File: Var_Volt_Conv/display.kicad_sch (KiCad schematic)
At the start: 9 parts

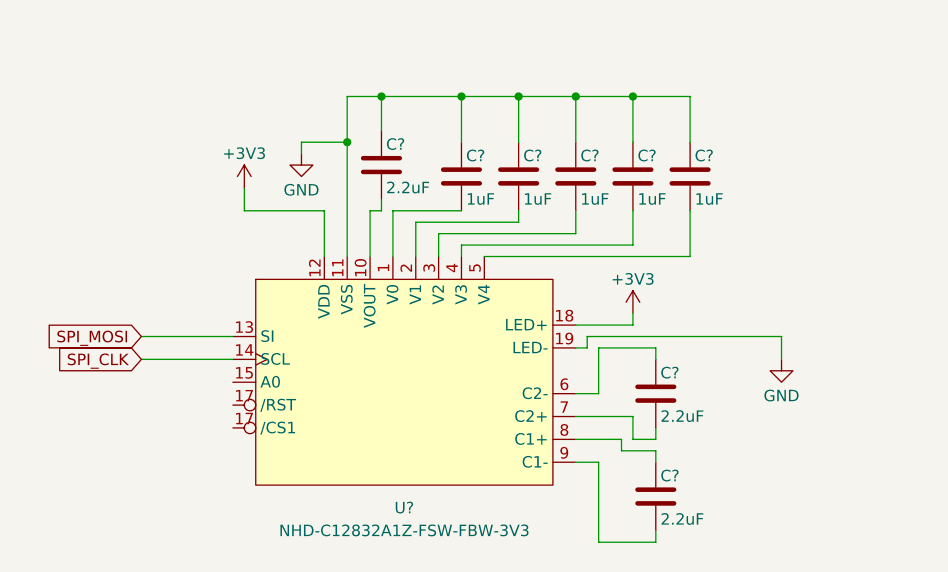
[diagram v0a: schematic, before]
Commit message: Tidied up microcontoller schematic
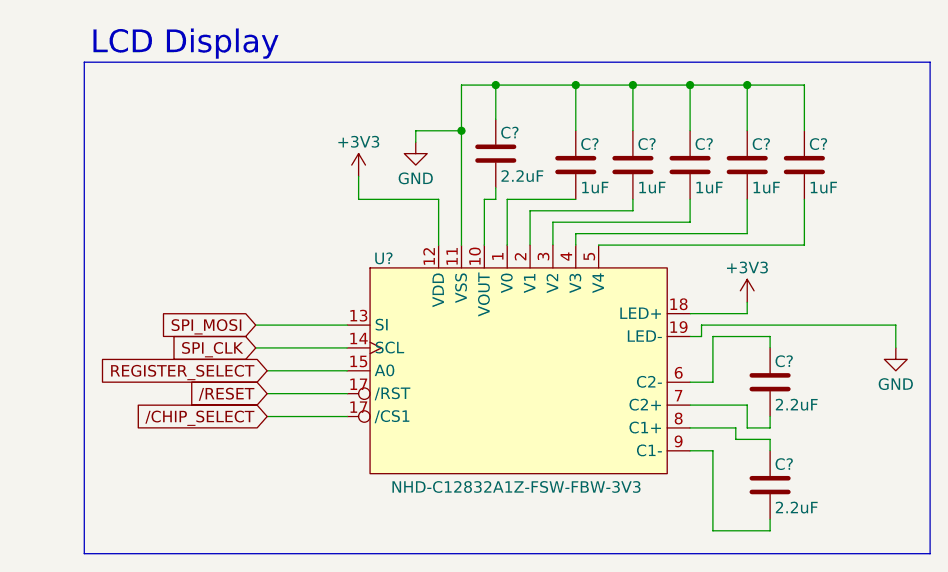
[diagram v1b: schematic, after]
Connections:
- net REGISTER_SELECT: now reaches U?.15 (A0)
- net /RESET: now reaches U?.17 (/RST)
- new net /CHIP_SELECT: U?.17 (/RST)
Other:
- note added: "LCD Display"
- moved on the sheet: C?, U?

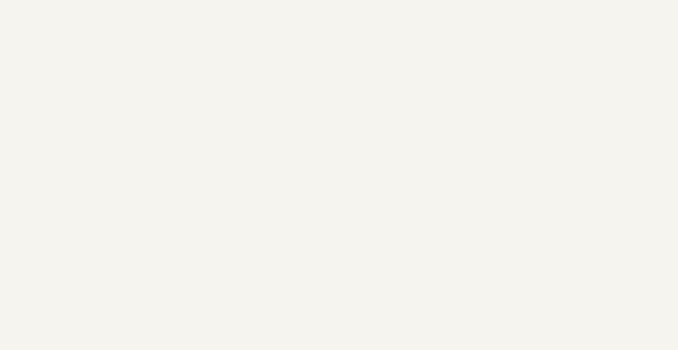
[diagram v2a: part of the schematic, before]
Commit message: Add bounding boxes and title/labels to all the sub-circuits
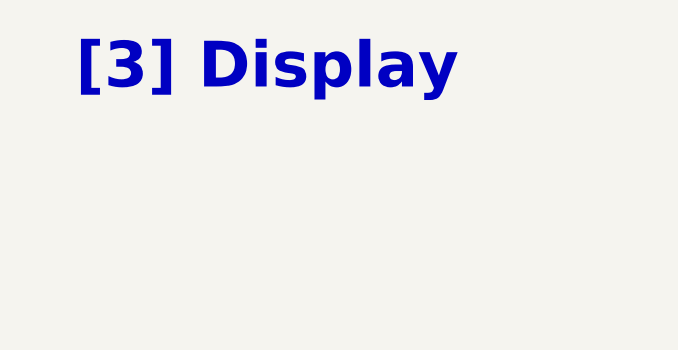
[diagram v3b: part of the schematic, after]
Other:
- note added: "[3] Display"
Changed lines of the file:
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@@
+		)
+	)
+	(text "[3] Display\n"
+		(exclude_from_sim no)
+		(at 44.45 25.654 0)
+		(effects
+			(font
+				(size 5.08 5.08)
+				(thickness 1.016)
+				(bold yes)
+			)
 		)
 	)

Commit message: LCD screen needs a nominal supply voltage of 3V, added a 3V LDOto the power circuitry, the LDO is powered by the buck converter
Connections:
- net +3V3 renamed +3V0
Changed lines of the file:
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@@
+	)
+	(symbol
+		(lib_id "power:+3V0")
+		(at 175.26 93.98 0)
+		(unit 1)
+		(exclude_from_sim no)
+		(in_bom yes)
+		(on_board yes)
+		(dnp no)
+		(property "Reference" "#PWR027"
+			(at 175.26 97.79 0)
+			(effects
+				(font
+					(size 1.27 1.27)
+				)
+				(hide yes)
+			)
+		)
+		(property "Value" "+3V0"
+			(at 175.26 90.17 0)
+			(effects
+				(font
+					(size 1.27 1.27)
+				)
+			)
+		)
+		(property "Footprint" ""
+			(at 175.26 93.98 0)
+			(effects
+				(font
+					(size 1.27 1.27)
+				)
+				(hide yes)
+			)
+		)
+		(property "Datasheet" ""
+			(at 175.26 93.98 0)
+			(effects
+				(font
+					(size 1.27 1.27)
+				)
+				(hide yes)
+			)
+		)
+		(property "Description" "Power symbol creates a global label with name \"+3V0\""
+			(at 175.26 93.98 0)
+			(effects
+				(font
+					(size 1.27 1.27)
+				)
+				(hide yes)
+			)
+		)
+		(pin "1"
+		)
+		(instances
+			(project "Var_Volt_Conv"
+				(path "/7c9580d6-c22f-4506-b9c3-9272e882c9fb/da7c3a55-ae2d-42a4-870c-c5ac34ec6e6a"
+					(reference "#PWR027")
+					(unit 1)
+				)
+			)
+		)
+	)
+	(symbol
+		(lib_id "power:+3V0")
+		(at 132.08 80.01 0)
+		(unit 1)
+		(exclude_from_sim no)
+		(in_bom yes)
+		(on_board yes)
+		(dnp no)
+		(property "Reference" "#PWR026"
+			(at 132.08 83.82 0)
+			(effects
+				(font
+					(size 1.27 1.27)
+				)
+				(hide yes)
+			)
+		)
+		(property "Value" "+3V0"
+			(at 132.08 76.2 0)
+			(effects
+				(font
+					(size 1.27 1.27)
+				)
+			)
+		)
+		(property "Footprint" ""
+			(at 132.08 80.01 0)
+			(effects
+				(font
+					(size 1.27 1.27)
+				)
+				(hide yes)
+			)
+		)
+		(property "Datasheet" ""
+			(at 132.08 80.01 0)
+			(effects
+				(font
+					(size 1.27 1.27)
+				)
+				(hide yes)
+			)
+		)
+		(property "Description" "Power symbol creates a global label with name \"+3V0\""
+			(at 132.08 80.01 0)
+			(effects
+				(font
+					(size 1.27 1.27)
+				)
+				(hide yes)
+			)
+		)
+		(pin "1"
+		)
+		(instances
+			(project "Var_Volt_Conv"
+				(path "/7c9580d6-c22f-4506-b9c3-9272e882c9fb/da7c3a55-ae2d-42a4-870c-c5ac34ec6e6a"
+					(reference "#PWR026")
+					(unit 1)
+				)
+			)
+		)
 	)
 	(symbol
@@
 					(unit 1)
 				)
-			)
-		)
-	)
-	(symbol
-		(lib_id "power:+3V3")
-		(at 132.08 80.01 0)
-		(unit 1)
-		(exclude_from_sim no)
-		(in_bom yes)
-		(on_board yes)
-		(dnp no)
-		(property "Reference" "#PWR044"
-			(at 132.08 83.82 0)
-			(effects
-				(font
-					(size 1.27 1.27)
-				)
-				(hide yes)
-			)
-		)
-		(property "Value" "+3V3"
-			(at 132.08 76.2 0)
-			(effects
-				(font
-					(size 1.27 1.27)
-				)
-			)
-		)
-		(property "Footprint" ""
-			(at 132.08 80.01 0)
-			(effects
-				(font
-					(size 1.27 1.27)
-				)
-				(hide yes)
-			)
-		)
-		(property "Datasheet" ""
-			(at 132.08 80.01 0)
-			(effects
-				(font
-					(size 1.27 1.27)
-				)
-				(hide yes)
-			)
-		)
-		(property "Description" "Power symbol creates a global label with name \"+3V3\""
-			(at 132.08 80.01 0)
-			(effects
-				(font
-					(size 1.27 1.27)
-				)
-				(hide yes)
-			)
-		)
-		(pin "1"
-		)
-		(instances
-			(project "Var_Volt_Conv"
-				(path "/7c9580d6-c22f-4506-b9c3-9272e882c9fb/da7c3a55-ae2d-42a4-870c-c5ac34ec6e6a"
-					(reference "#PWR044")
-					(unit 1)
-				)
-			)
-		)
-	)
-	(symbol
-		(lib_id "power:+3V3")
-		(at 175.26 93.98 0)
-		(unit 1)
-		(exclude_from_sim no)
-		(in_bom yes)
-		(on_board yes)
-		(dnp no)
-		(property "Reference" "#PWR046"
-			(at 175.26 97.79 0)
-			(effects
-				(font
-					(size 1.27 1.27)
-				)
-				(hide yes)
-			)
-		)
-		(property "Value" "+3V3"
-			(at 175.26 90.17 0)
-			(effects
-				(font
-					(size 1.27 1.27)
-				)
-			)
-		)
-		(property "Footprint" ""
-			(at 175.26 93.98 0)
-			(effects
-				(font
-					(size 1.27 1.27)
-				)
-				(hide yes)
-			)
-		)
-		(property "Datasheet" ""
-			(at 175.26 93.98 0)
-			(effects
-				(font
-					(size 1.27 1.27)
-				)
-				(hide yes)
-			)
-		)
-		(property "Description" "Power symbol creates a global label with name \"+3V3\""
-			(at 175.26 93.98 0)
-			(effects
-				(font
-					(size 1.27 1.27)
-				)
-				(hide yes)
-			)
-		)
-		(pin "1"
-		)
-		(instances
-			(project "Var_Volt_Conv"
-				(path "/7c9580d6-c22f-4506-b9c3-9272e882c9fb/da7c3a55-ae2d-42a4-870c-c5ac34ec6e6a"
-					(reference "#PWR046")
-					(unit 1)
-				)

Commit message: Annotated schematic symbols
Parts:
- gave numbers to parts that had none: 9
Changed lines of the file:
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@@
 		(on_board yes)
 		(dnp no)
-		(property "Reference" "C?"
+		(property "Reference" "C306"
 			(at 182.118 76.454 0)
 			(effects
@@
 			(project "Var_Volt_Conv"
 				(path "/7c9580d6-c22f-4506-b9c3-9272e882c9fb/da7c3a55-ae2d-42a4-870c-c5ac34ec6e6a"
-					(reference "C?")
+					(reference "C306")
 					(unit 1)
 				)
@@
 		(on_board yes)
 		(dnp no)
-		(property "Reference" "C?"
+		(property "Reference" "C302"
 			(at 156.718 76.454 0)
 			(effects
@@
 			(project "Var_Volt_Conv"
 				(path "/7c9580d6-c22f-4506-b9c3-9272e882c9fb/da7c3a55-ae2d-42a4-870c-c5ac34ec6e6a"
-					(reference "C?")
+					(reference "C302")
 					(unit 1)
 				)
@@
 		(on_board yes)
 		(dnp no)
-		(property "Reference" "C?"
+		(property "Reference" "C304"
 			(at 169.418 76.454 0)
 			(effects
@@
 			(project "Var_Volt_Conv"
 				(path "/7c9580d6-c22f-4506-b9c3-9272e882c9fb/da7c3a55-ae2d-42a4-870c-c5ac34ec6e6a"
-					(reference "C?")
+					(reference "C304")
 					(unit 1)
 				)
@@
 		(on_board yes)
 		(dnp no)
-		(property "Reference" "C?"
+		(property "Reference" "C308"
 			(at 178.308 112.014 0)
 			(effects
@@
 			(project "Var_Volt_Conv"
 				(path "/7c9580d6-c22f-4506-b9c3-9272e882c9fb/da7c3a55-ae2d-42a4-870c-c5ac34ec6e6a"
-					(reference "C?")
+					(reference "C308")
 					(unit 1)
 				)
@@
 		(on_board yes)
 		(dnp no)
-		(property "Reference" "U?"
+		(property "Reference" "U301"
 			(at 134.874 89.154 0)
 			(effects
@@
 			(project ""
 				(path "/7c9580d6-c22f-4506-b9c3-9272e882c9fb/da7c3a55-ae2d-42a4-870c-c5ac34ec6e6a"
-					(reference "U?")
+					(reference "U301")
 					(unit 1)
 				)
@@
 		(on_board yes)
 		(dnp no)
-		(property "Reference" "C?"
+		(property "Reference" "C303"
 			(at 163.068 76.454 0)
 			(effects
@@
 			(project "Var_Volt_Conv"
 				(path "/7c9580d6-c22f-4506-b9c3-9272e882c9fb/da7c3a55-ae2d-42a4-870c-c5ac34ec6e6a"
-					(reference "C?")
+					(reference "C303")
 					(unit 1)
 				)
@@
 		(on_board yes)
 		(dnp no)
-		(property "Reference" "C?"
+		(property "Reference" "C305"
 			(at 175.768 76.454 0)
 			(effects
@@
 			(project "Var_Volt_Conv"
 				(path "/7c9580d6-c22f-4506-b9c3-9272e882c9fb/da7c3a55-ae2d-42a4-870c-c5ac34ec6e6a"
-					(reference "C?")
+					(reference "C305")
 					(unit 1)
 				)
@@
 		(on_board yes)
 		(dnp no)
-		(property "Reference" "C?"
+		(property "Reference" "C307"
 			(at 178.308 100.584 0)
 			(effects
@@
 			(project "Var_Volt_Conv"
 				(path "/7c9580d6-c22f-4506-b9c3-9272e882c9fb/da7c3a55-ae2d-42a4-870c-c5ac34ec6e6a"
-					(reference "C?")
+					(reference "C307")
 					(unit 1)
 				)
@@
 		(on_board yes)
 		(dnp no)
-		(property "Reference" "C?"
+		(property "Reference" "C301"
 			(at 147.828 75.184 0)
 			(effects
@@
 			(project "Var_Volt_Conv"
 				(path "/7c9580d6-c22f-4506-b9c3-9272e882c9fb/da7c3a55-ae2d-42a4-870c-c5ac34ec6e6a"
-					(reference "C?")
-					(unit 1)
-				)
+					(reference "C301")
+					(unit 1)
+				)

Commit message: Fixed ERC issues
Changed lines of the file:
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@@
 		(on_board yes)
 		(dnp no)
-		(property "Reference" "#PWR047"
+		(property "Reference" "#PWR0304"
 			(at 191.77 105.41 0)
 			(effects
@@
 			(project "Var_Volt_Conv"
 				(path "/7c9580d6-c22f-4506-b9c3-9272e882c9fb/da7c3a55-ae2d-42a4-870c-c5ac34ec6e6a"
-					(reference "#PWR047")
+					(reference "#PWR0304")
 					(unit 1)
 				)
@@
 		(on_board yes)
 		(dnp no)
-		(property "Reference" "#PWR027"
+		(property "Reference" "#PWR0303"
 			(at 175.26 97.79 0)
 			(effects
@@
 			(project "Var_Volt_Conv"
 				(path "/7c9580d6-c22f-4506-b9c3-9272e882c9fb/da7c3a55-ae2d-42a4-870c-c5ac34ec6e6a"
-					(reference "#PWR027")
+					(reference "#PWR0303")
 					(unit 1)
 				)
@@
 		(on_board yes)
 		(dnp no)
-		(property "Reference" "#PWR026"
+		(property "Reference" "#PWR0302"
 			(at 132.08 83.82 0)
 			(effects
@@
 			(project "Var_Volt_Conv"
 				(path "/7c9580d6-c22f-4506-b9c3-9272e882c9fb/da7c3a55-ae2d-42a4-870c-c5ac34ec6e6a"
-					(reference "#PWR026")
+					(reference "#PWR0302")
 					(unit 1)
 				)
@@
 		(on_board yes)
 		(dnp no)
+		(fields_autoplaced yes)
 		(property "Reference" "U301"
-			(at 134.874 89.154 0)
+			(at 149.86 115.57 0)
 			(effects
 				(font
@@
 		)
 		(property "Value" "NHD-C12832A1Z-FSW-FBW-3V3"
-			(at 149.606 114.554 0)
+			(at 149.86 118.11 0)
 			(effects
 				(font
@@
 			)
 		)
+		(pin "10"
+		)
 		(pin "4"
 		)
+		(pin "5"
+		)
+		(pin "19"
+		)
 		(pin "6"
 		)
+		(pin "15"
+		)
+		(pin "13"
+		)
+		(pin "18"
+		)
+		(pin "8"
+		)
+		(pin "17"
+		)
+		(pin "11"
+		)
 		(pin "9"
 		)
-		(pin "11"
+		(pin "2"
 		)
 		(pin "1"
@@
 		(pin "3"
 		)
-		(pin "8"
+		(pin "14"
 		)
 		(pin "17"
 		)
-		(pin "2"
-		)
-		(pin "17"
-		)
-		(pin "5"
-		)
-		(pin "10"
+		(pin "12"
 		)
 		(pin "7"
-		)
-		(pin "14"
-		)
-		(pin "15"
-		)
-		(pin "12"
-		)
-		(pin "13"
-		)
-		(pin "18"
-		)
-		(pin "19"
 		)
 		(instances
@@
 		(on_board yes)
 		(dnp no)
-		(property "Reference" "#PWR045"
+		(property "Reference" "#PWR0301"
 			(at 138.43 82.55 0)
 			(effects
@@
 			(project "Var_Volt_Conv"
 				(path "/7c9580d6-c22f-4506-b9c3-9272e882c9fb/da7c3a55-ae2d-42a4-870c-c5ac34ec6e6a"
-					(reference "#PWR045")
-					(unit 1)
-				)
+					(reference "#PWR0301")
+					(unit 1)
+				)

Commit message: Add footprints and correct LCD pin numbering
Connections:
- net /RESET: now also U301.16 (/RST); no longer U301.17 (/RST)
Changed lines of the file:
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@@
-	)
-	(symbol
-		(lib_id "power:+3V0")
-		(at 175.26 93.98 0)
-		(unit 1)
-		(exclude_from_sim no)
-		(in_bom yes)
-		(on_board yes)
-		(dnp no)
-		(property "Reference" "#PWR0303"
-			(at 175.26 97.79 0)
-			(effects
-				(font
-					(size 1.27 1.27)
-				)
-				(hide yes)
-			)
-		)
-		(property "Value" "+3V0"
-			(at 175.26 90.17 0)
-			(effects
-				(font
-					(size 1.27 1.27)
-				)
-			)
-		)
-		(property "Footprint" ""
-			(at 175.26 93.98 0)
-			(effects
-				(font
-					(size 1.27 1.27)
-				)
-				(hide yes)
-			)
-		)
-		(property "Datasheet" ""
-			(at 175.26 93.98 0)
-			(effects
-				(font
-					(size 1.27 1.27)
-				)
-				(hide yes)
-			)
-		)
-		(property "Description" "Power symbol creates a global label with name \"+3V0\""
-			(at 175.26 93.98 0)
-			(effects
-				(font
-					(size 1.27 1.27)
-				)
-				(hide yes)
-			)
-		)
-		(pin "1"
-		)
-		(instances
-			(project "Var_Volt_Conv"
-				(path "/7c9580d6-c22f-4506-b9c3-9272e882c9fb/da7c3a55-ae2d-42a4-870c-c5ac34ec6e6a"
-					(reference "#PWR0303")
-					(unit 1)
-				)
-			)
-		)
-	)
-	(symbol
-		(lib_id "power:+3V0")
-		(at 132.08 80.01 0)
-		(unit 1)
-		(exclude_from_sim no)
-		(in_bom yes)
-		(on_board yes)
-		(dnp no)
-		(property "Reference" "#PWR0302"
-			(at 132.08 83.82 0)
-			(effects
-				(font
-					(size 1.27 1.27)
-				)
-				(hide yes)
-			)
-		)
-		(property "Value" "+3V0"
-			(at 132.08 76.2 0)
-			(effects
-				(font
-					(size 1.27 1.27)
-				)
-			)
-		)
-		(property "Footprint" ""
-			(at 132.08 80.01 0)
-			(effects
-				(font
-					(size 1.27 1.27)
-				)
-				(hide yes)
-			)
-		)
-		(property "Datasheet" ""
-			(at 132.08 80.01 0)
-			(effects
-				(font
-					(size 1.27 1.27)
-				)
-				(hide yes)
-			)
-		)
-		(property "Description" "Power symbol creates a global label with name \"+3V0\""
-			(at 132.08 80.01 0)
-			(effects
-				(font
-					(size 1.27 1.27)
-				)
-				(hide yes)
-			)
-		)
-		(pin "1"
-		)
-		(instances
-			(project "Var_Volt_Conv"
-				(path "/7c9580d6-c22f-4506-b9c3-9272e882c9fb/da7c3a55-ae2d-42a4-870c-c5ac34ec6e6a"
-					(reference "#PWR0302")
-					(unit 1)
-				)
-			)
-		)
 	)
 	(symbol
@@
 			)
 		)
+		(pin "11"
+		)
+		(pin "18"
+		)
+		(pin "12"
+		)
+		(pin "13"
+		)
+		(pin "14"
+		)
+		(pin "16"
+		)
+		(pin "19"
+		)
+		(pin "9"
+		)
+		(pin "1"
+		)
 		(pin "10"
 		)
+		(pin "15"
+		)
+		(pin "17"
+		)
+		(pin "3"
+		)
 		(pin "4"
 		)
 		(pin "5"
 		)
-		(pin "19"
+		(pin "8"
 		)
 		(pin "6"
 		)
-		(pin "15"
-		)
-		(pin "13"
-		)
-		(pin "18"
-		)
-		(pin "8"
-		)
-		(pin "17"
-		)
-		(pin "11"
-		)
-		(pin "9"
-		)
 		(pin "2"
-		)
-		(pin "1"
-		)
-		(pin "3"
-		)
-		(pin "14"
-		)
-		(pin "17"
-		)
-		(pin "12"
 		)
 		(pin "7"
@@
 					(unit 1)
 				)
+			)
+		)
+	)
+	(symbol
+		(lib_id "power:+3V0")
+		(at 175.26 93.98 0)
+		(unit 1)
+		(exclude_from_sim no)
+		(in_bom yes)
+		(on_board yes)
+		(dnp no)
+		(property "Reference" "#PWR0303"
+			(at 175.26 97.79 0)
+			(effects
+				(font
+					(size 1.27 1.27)
+				)
+				(hide yes)
+			)
+		)
+		(property "Value" "+3V0"
+			(at 175.26 90.17 0)
+			(effects
+				(font
+					(size 1.27 1.27)
+				)
+			)
+		)
+		(property "Footprint" ""
+			(at 175.26 93.98 0)
+			(effects
+				(font
+					(size 1.27 1.27)
+				)
+				(hide yes)
+			)
+		)
+		(property "Datasheet" ""
+			(at 175.26 93.98 0)
+			(effects
+				(font
+					(size 1.27 1.27)
+				)
+				(hide yes)
+			)
+		)
+		(property "Description" "Power symbol creates a global label with name \"+3V0\""
+			(at 175.26 93.98 0)
+			(effects
+				(font
+					(size 1.27 1.27)
+				)
+				(hide yes)
+			)
+		)
+		(pin "1"
+		)
+		(instances
+			(project "Var_Volt_Conv"
+				(path "/7c9580d6-c22f-4506-b9c3-9272e882c9fb/da7c3a55-ae2d-42a4-870c-c5ac34ec6e6a"
+					(reference "#PWR0303")
+					(unit 1)
+				)
+			)
+		)
+	)
+	(symbol
+		(lib_id "power:+3V0")
+		(at 132.08 80.01 0)
+		(unit 1)
+		(exclude_from_sim no)
+		(in_bom yes)
+		(on_board yes)
+		(dnp no)
+		(property "Reference" "#PWR0302"
+			(at 132.08 83.82 0)
+			(effects
+				(font
+					(size 1.27 1.27)
+				)
+				(hide yes)
+			)
+		)
+		(property "Value" "+3V0"
+			(at 132.08 76.2 0)
+			(effects
+				(font
+					(size 1.27 1.27)
+				)
+			)
+		)
+		(property "Footprint" ""
+			(at 132.08 80.01 0)
+			(effects
+				(font
+					(size 1.27 1.27)
+				)
+				(hide yes)
+			)
+		)
+		(property "Datasheet" ""
+			(at 132.08 80.01 0)
+			(effects
+				(font
+					(size 1.27 1.27)
+				)
+				(hide yes)
+			)
+		)
+		(property "Description" "Power symbol creates a global label with name \"+3V0\""
+			(at 132.08 80.01 0)
+			(effects
+				(font
+					(size 1.27 1.27)
+				)
+				(hide yes)
+			)
+		)
+		(pin "1"
+		)
+		(instances
+			(project "Var_Volt_Conv"
+				(path "/7c9580d6-c22f-4506-b9c3-9272e882c9fb/da7c3a55-ae2d-42a4-870c-c5ac34ec6e6a"
+					(reference "#PWR0302")
+					(unit 1)
+				)

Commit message: Add filter caps to current sensors
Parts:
- U301: footprint (none) -> Display:NHD-C12832A1Z-FSRGB
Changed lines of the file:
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@@
 			)
 		)
-		(property "Footprint" ""
+		(property "Footprint" "Display:NHD-C12832A1Z-FSRGB"
 			(at 148.59 87.63 90)
 			(effects
